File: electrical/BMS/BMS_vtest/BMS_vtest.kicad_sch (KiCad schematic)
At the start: 7 parts, among them Q1 NMOS, U1 STM32F103C4Tx, U2 BQ79612PAPRQ1

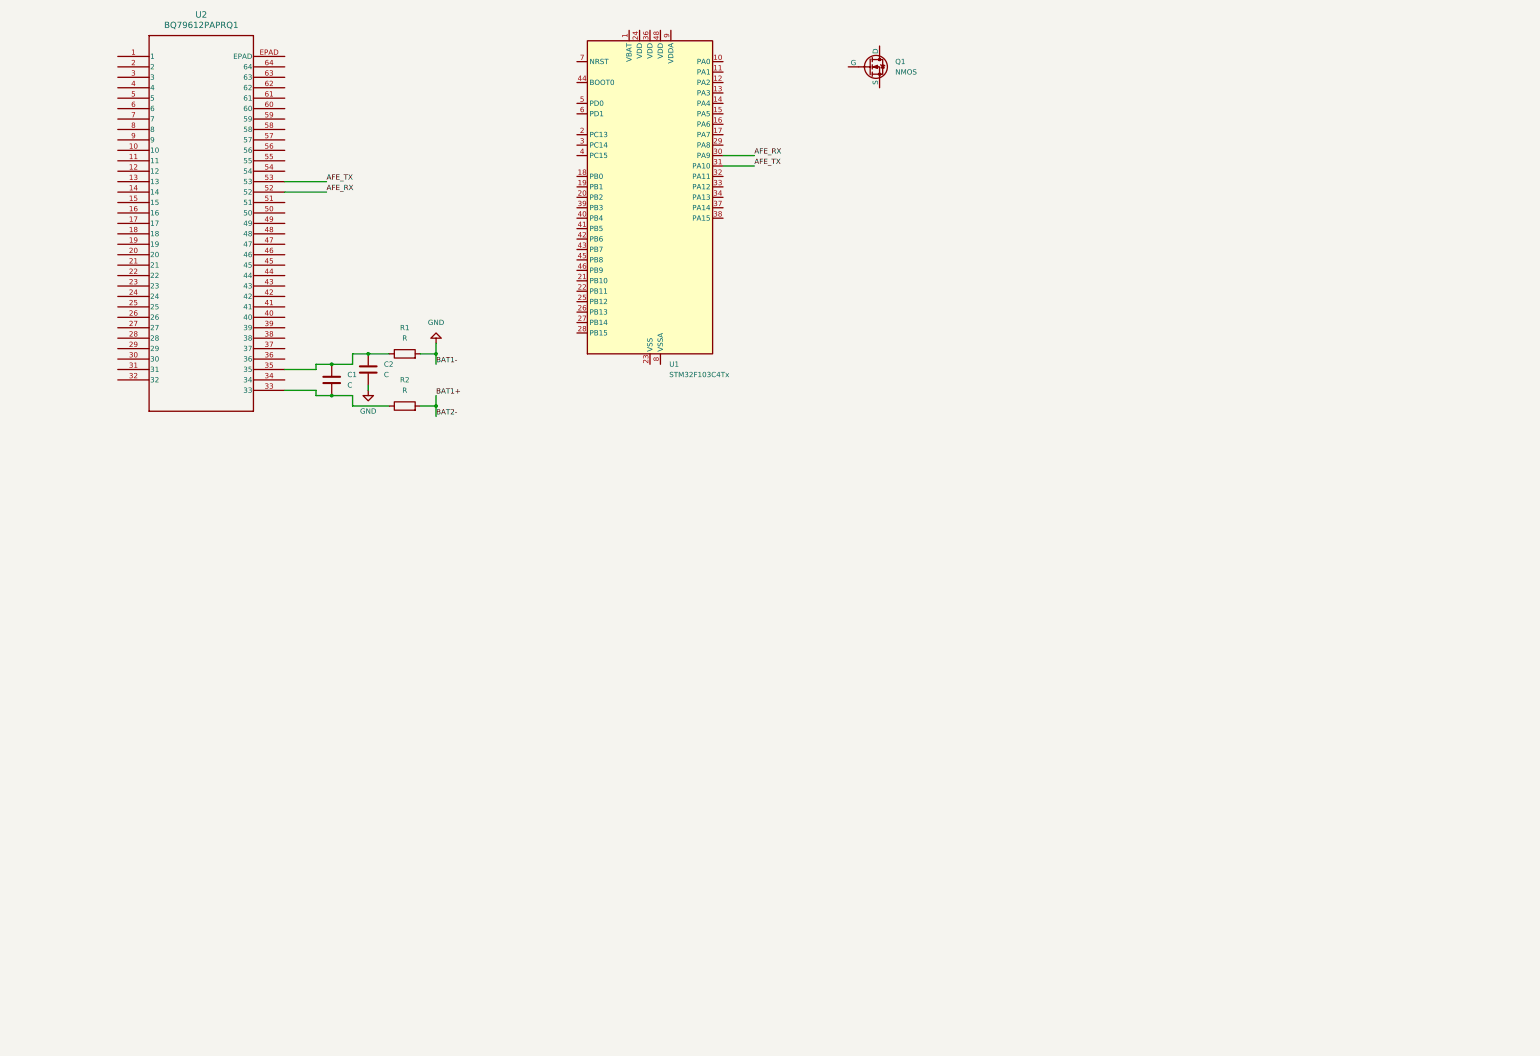
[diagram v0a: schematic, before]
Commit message: cell balancing circuitry
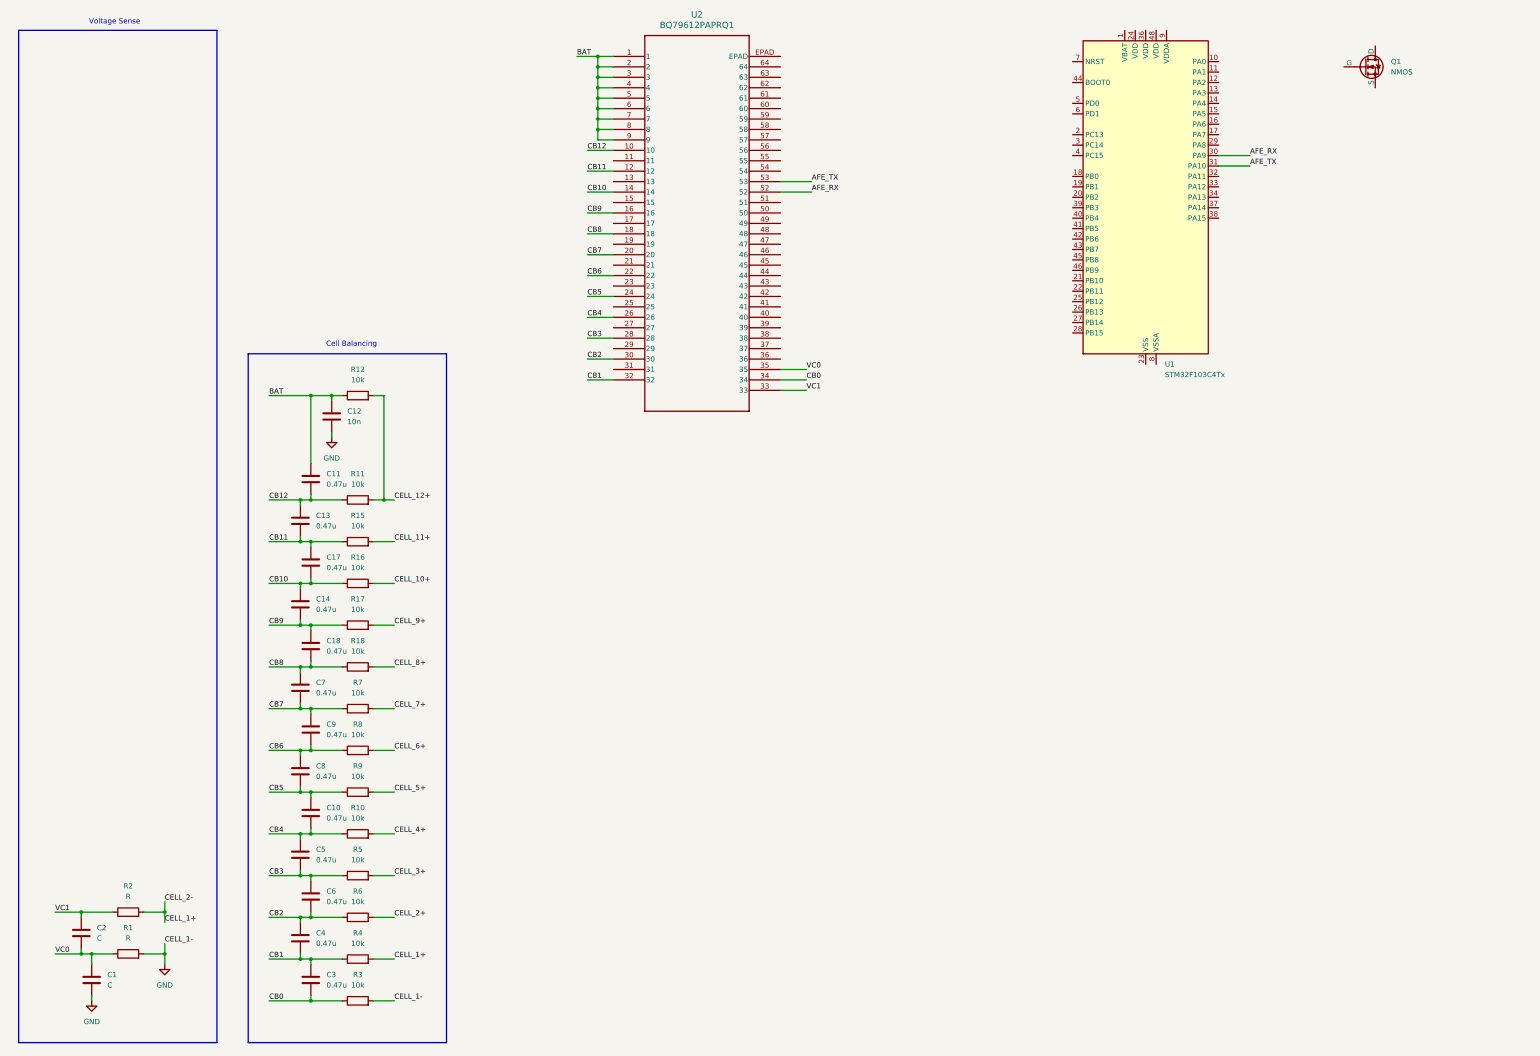
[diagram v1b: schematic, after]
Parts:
- added C10, C11, C13, C14, C17, C18, C3, C4, C5, C6, C7, C8, C9: 0.47u, symbol Device:C
- added C12: 10n, symbol Device:C
- added R10, R11, R12, R15, R16, R17, R18, R3, R4, R5, R6, R7, R8, R9: 10k, symbol Device:R
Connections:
- net GND: now also C1.2, C12.2, R3.2; no longer C2.2
- net VC0: now reaches C1.1, R1.1, U2.35
- net VC0: now also C2.2; no longer C2.1
- net VC1: now reaches R2.1, U2.33
- net VC1: now also C2.1; no longer C1.2
- net BAT: now reaches U2.1
- net BAT: now also U2.2, U2.3, U2.4, U2.5, U2.6, U2.7, U2.8, U2.9, C11.1, C12.1, R12.1
- net CB12: now reaches U2.10
- net CB12: now also C11.2, C13.1, R11.1
- net CB11: now reaches U2.12
- net CB11: now also C13.2, C17.1, R15.1
- net CB10: now reaches U2.14
- net CB10: now also C14.1, C17.2, R16.1
- net CB9: now reaches U2.16
- net CB9: now also C14.2, C18.1, R17.1
- net CB8: now reaches U2.18
- net CB8: now also C18.2, C7.1, R18.1
- net CB7: now reaches U2.20
- net CB7: now also C7.2, C9.1, R7.1
- net CB6: now reaches U2.22
- net CB6: now also C8.1, C9.2, R8.1
- net CB5: now reaches U2.24
- net CB5: now also C10.1, C8.2, R9.1
- net CB4: now reaches U2.26
- net CB4: now also C10.2, C5.1, R10.1
- net CB3: now reaches U2.28
- net CB3: now also C5.2, C6.1, R5.1
- net CB2: now reaches U2.30
- net CB2: now also C4.1, C6.2, R6.1
- net CB1: now reaches U2.32
- net CB1: now also C3.1, C4.2, R4.1
- net CB0: now reaches U2.34
- net CB0: now also C3.2, R3.1
- net BAT1+ renamed CELL_1+
- net CELL_1+: now also R4.2
- new net CELL_10+: R16.2
- new net CELL_11+: R15.2
- new net CELL_12+: R11.2, R12.2
- new net CELL_2+: R6.2
- new net CELL_3+: R5.2
- new net CELL_4+: R10.2
- new net CELL_5+: R9.2
- new net CELL_6+: R8.2
- new net CELL_7+: R7.2
- new net CELL_8+: R18.2
- new net CELL_9+: R17.2
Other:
- note added: "Cell Balancing"
- note added: "Voltage Sense"
- moved on the sheet: Q1, U1, U2

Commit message: voltage sense circuitry
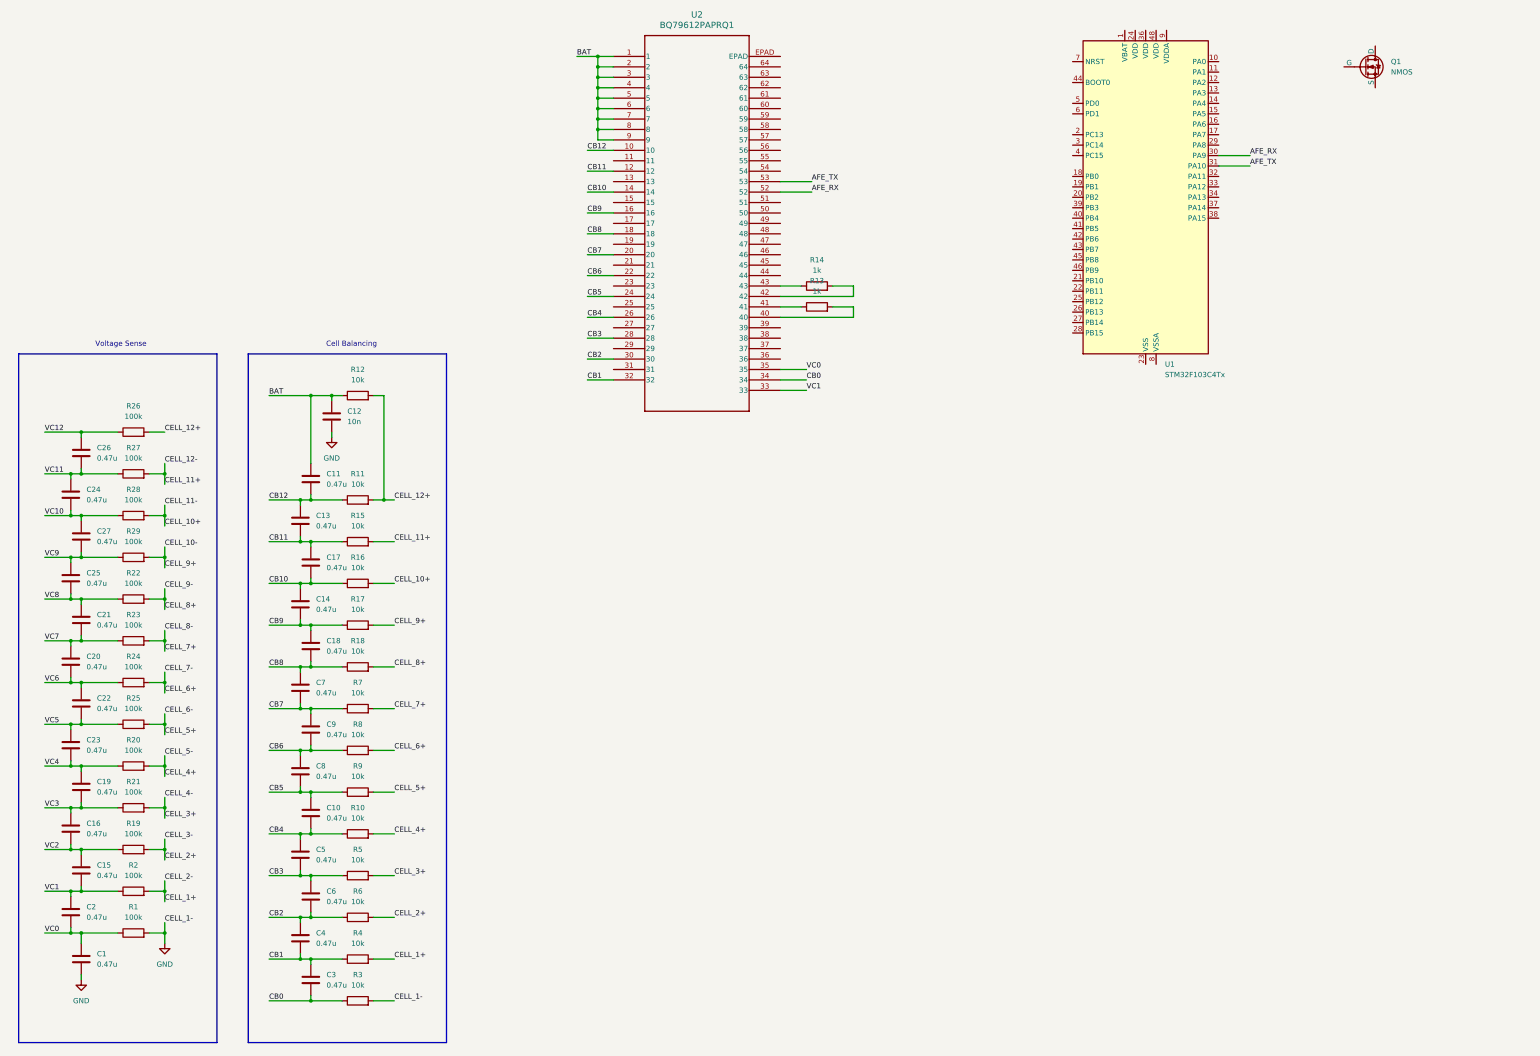
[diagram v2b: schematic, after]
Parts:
- added C15, C16, C19, C20, C21, C22, C23, C24, C25, C26, C27: 0.47u, symbol Device:C
- added R13, R14: 1k, symbol Device:R
- added R19, R20, R21, R22, R23, R24, R25, R26, R27, R28, R29: 100k, symbol Device:R
- C1, C2: value C -> 0.47u
- R1, R2: value R -> 100k
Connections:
- net CELL_10+: now also R28.2
- net CELL_11+: now also R27.2
- net CELL_12+: now also R26.2
- net CELL_2+: now also R19.2
- net CELL_3+: now also R21.2
- net CELL_4+: now also R20.2
- net CELL_5+: now also R25.2
- net CELL_6+: now also R24.2
- net CELL_7+: now also R23.2
- net CELL_8+: now also R22.2
- net VC1: now also C15.2
- net at U2.40: now also R13.2
- net at U2.41: now also R13.1
- net at U2.42: now also R14.2
- net at U2.43: now also R14.1
- net CELL_9+ renamed CELL_10-
- net CELL_10-: now also R29.2
- new net VC10: C24.2, C27.1, R28.1
- new net VC11: C24.1, C26.2, R27.1
- new net VC12: C26.1, R26.1
- new net VC2: C15.1, C16.2, R19.1
- new net VC3: C16.1, C19.2, R21.1
- new net VC4: C19.1, C23.2, R20.1
- new net VC5: C22.2, C23.1, R25.1
- new net VC6: C20.2, C22.1, R24.1
- new net VC7: C20.1, C21.2, R23.1
- new net VC8: C21.1, C25.2, R22.1
- new net VC9: C25.1, C27.2, R29.1
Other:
- moved on the sheet: C1, C2, R1, R2

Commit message: grounding
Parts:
- added C28, C34: 0.1u, symbol Device:C
- added C29: 0.22u, symbol Device:C
- added C30: 4.7u, symbol Device:C
- added C31: 2.2u, symbol Device:C
- added C32, C33: 1u, symbol Device:C
- added Q2: NPN, symbol Simulation_SPICE:NPN
- added R30: 100, symbol Device:R
- added R31: 200, symbol Device:R
- R12: value 10k -> 30k
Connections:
- net CELL_12+: now also R31.2
- net GND: now also U2.36, U2.39, U2.46, U2.50, C28.1, C29.2, C30.2, C31.2, C32.2, C33.2, C34.1
- net VC10: now also U2.15
- net VC11: now also U2.13
- net VC12: now also U2.11
- net VC2: now also U2.31
- net VC3: now also U2.29
- net VC4: now also U2.27
- net VC5: now also U2.25
- net VC6: now also U2.23
- net VC7: now also U2.21
- net VC8: now also U2.19
- net VC9: now also U2.17
- net REFHP: now reaches U2.37
- net REFHP: now also C32.1
- net AVDD: now reaches U2.38
- net AVDD: now also C33.1
- net NEG5V: now reaches U2.44
- net NEG5V: now also C34.2
- net CVDD: now reaches U2.45
- net CVDD: now also C30.1
- net LDOIN: now reaches U2.47
- net LDOIN: now also C28.2, Q2.3 (E)
- net NPNB: now reaches U2.48
- net NPNB: now also Q2.2 (B)
- net DVDD: now reaches U2.49
- net DVDD: now also C31.1
- new net: C29.1, Q2.1 (C), R30.1
- new net: R30.2, R31.1
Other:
- note added: "(STM) Load Switch"
- moved on the sheet: C1, C10, C11, C12, C13, C14, C15, C16, C17, C18, C19, C2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

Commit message: temperature sensing for pcb and mosfet
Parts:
- added C35: 1u, symbol Device:C
- added R32, R33: 100k, symbol Device:R
- added R34: 10k, symbol Device:R
- added R35: 3.6k, symbol Device:R
- added R36: 15k, symbol Device:R
- added TH1, TH2: Thermistor_NTC, symbol Device:Thermistor_NTC
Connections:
- net AFE_RX: now also R32.2
- net AFE_TX: now also R33.2
- net CVDD: now also R32.1
- net GND: now also C35.2, R36.2, TH1.2, TH2.2
- net TSREF: now reaches U2.51
- net TSREF: now also C35.1, R34.1, R35.1
- net VDD1: now reaches U1.24 (VDD)
- net VDD1: now also R33.1
- new net GPIO2: R34.2, TH1.1
- new net GPIO3: R35.2, R36.1, TH2.1
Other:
- note added: "MOSFET (2) and PCB Cell Balancing (3)"
- note added: "Temperature Sensing"
